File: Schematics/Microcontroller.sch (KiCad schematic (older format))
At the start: 25 parts, among them CON1 USB-MICRO-B, IC1 ATXMEGA256A3BU-A, J1 AVR_JTAG_Header, SW1 SW_PUSH, SW2 SW_PUSH, X1 16MHz, X2 32.768KhZ

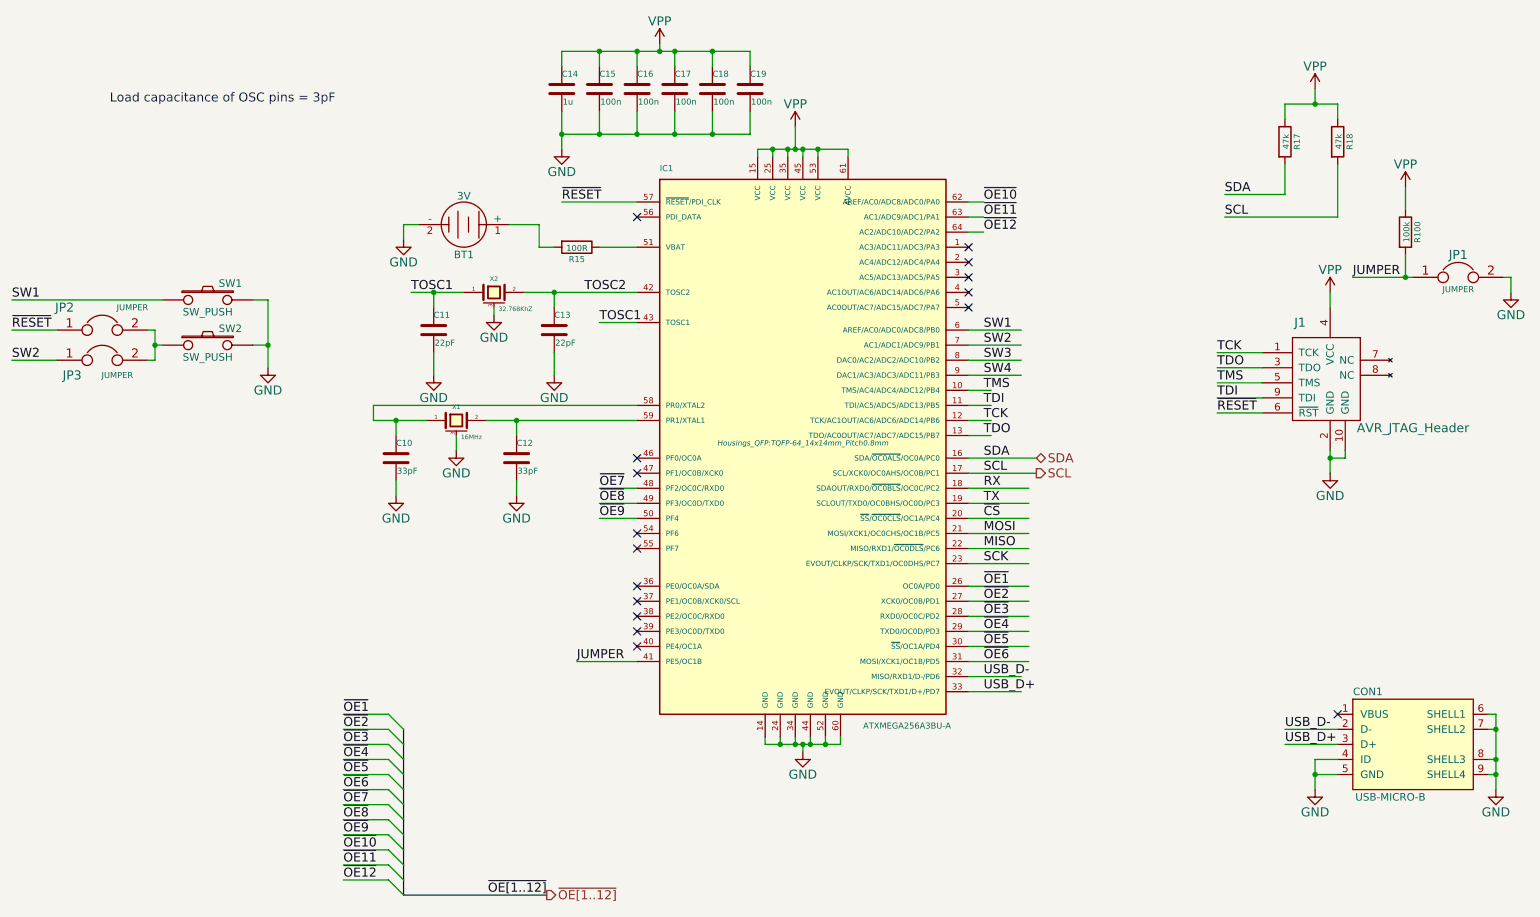
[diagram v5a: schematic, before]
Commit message: Split design into two modules
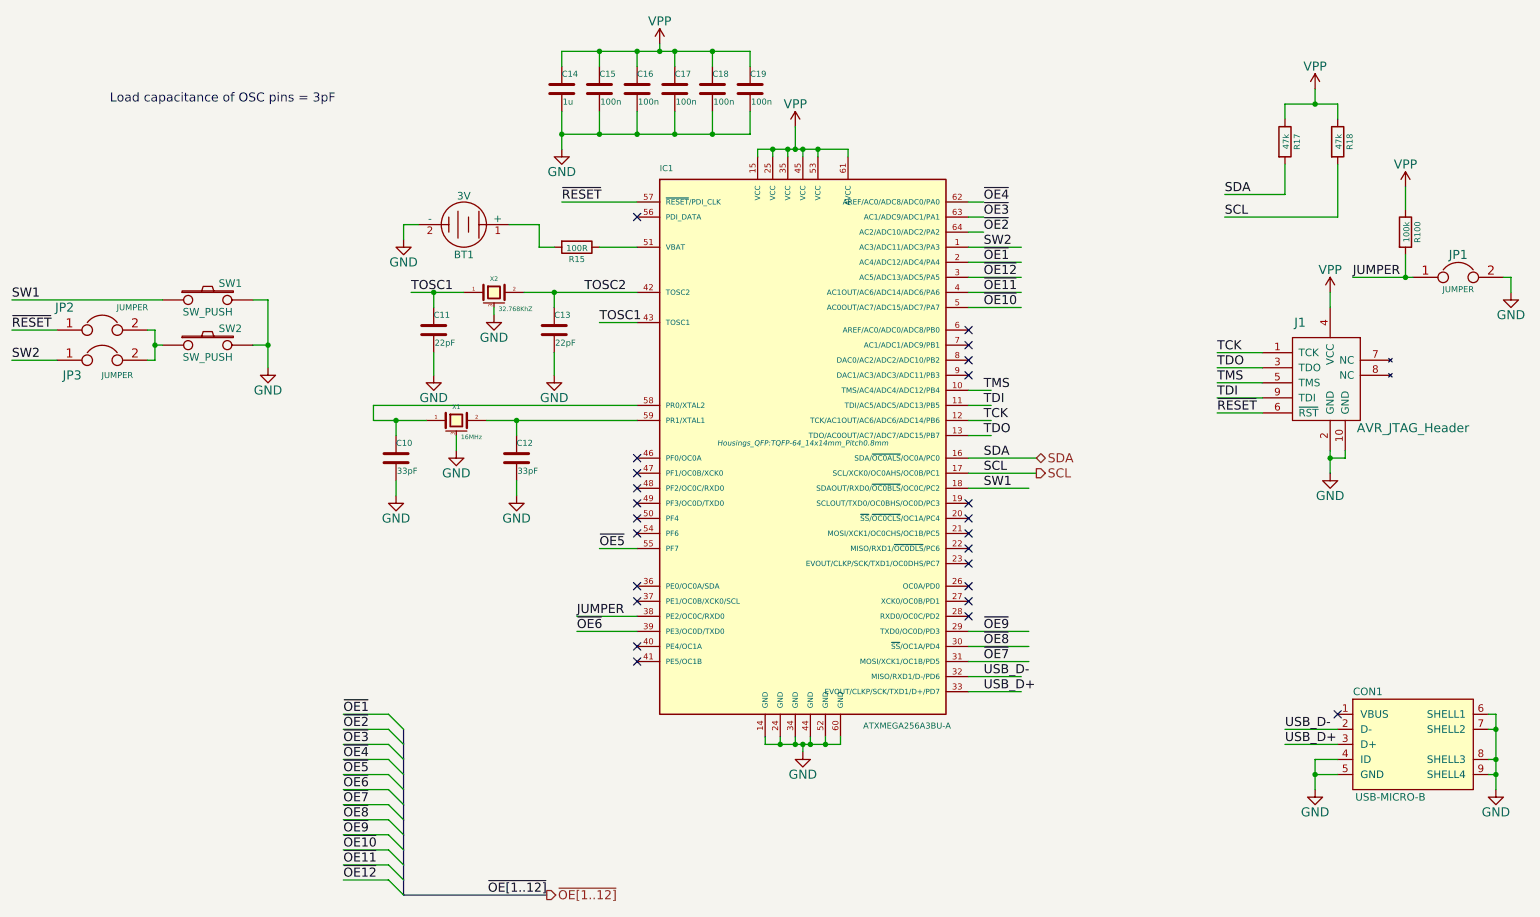
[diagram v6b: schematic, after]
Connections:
- net labels removed: MISO, MOSI, RX, SCK, SW3, SW4, TX, ~CS
- wire segments 174 -> 133
- no-connect marks 16 -> 24
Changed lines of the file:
@@
 	1    0    0    -1
 $EndComp
-Text Label 7050 4500 0    60   ~ 0
+Text Label 7050 2350 0    60   ~ 0
 ~OE1
-Text Label 7050 4600 0    60   ~ 0
+Text Label 7050 2150 0    60   ~ 0
 ~OE2
-Text Label 7050 4700 0    60   ~ 0
+Text Label 7050 2050 0    60   ~ 0
 ~OE3
+Text Label 7050 1950 0    60   ~ 0
+~OE4
+Text Label 4500 4250 0    60   ~ 0
+~OE5
+Text Label 4350 4800 0    60   ~ 0
+~OE6
+Text Label 7050 5000 0    60   ~ 0
+~OE7
+Text Label 7050 4900 0    60   ~ 0
+~OE8
 Text Label 7050 4800 0    60   ~ 0
-~OE4
-Text Label 7050 4900 0    60   ~ 0
-~OE5
-Text Label 7050 5000 0    60   ~ 0
-~OE6
-Text Label 4500 3850 0    60   ~ 0
-~OE7
-Text Label 4500 3950 0    60   ~ 0
-~OE8
-Text Label 4500 4050 0    60   ~ 0
 ~OE9
-Text Label 7050 1950 0    60   ~ 0
+Text Label 7050 2650 0    60   ~ 0
 ~OE10
-Text Label 7050 2050 0    60   ~ 0
+Text Label 7050 2550 0    60   ~ 0
 ~OE11
-Text Label 7050 2150 0    60   ~ 0
+Text Label 7050 2450 0    60   ~ 0
 ~OE12
 Entry Wire Line
@@
 	1    0    0    -1
 $EndComp
-Text Label 7050 4350 0    60   ~ 0
-SCK
-Text Label 7050 4250 0    60   ~ 0
-MISO
-Text Label 7050 4150 0    60   ~ 0
-MOSI
-Text Label 7050 4050 0    60   ~ 0
-~CS
-Text Label 7050 3950 0    60   ~ 0
-TX
-Text Label 7050 3850 0    60   ~ 0
-RX
-NoConn ~ 4750 4250
 NoConn ~ 4750 4150
 NoConn ~ 4750 3750
 NoConn ~ 4750 3650
-NoConn ~ 6950 2450
 NoConn ~ 9400 5350
 $Comp
@@
 	9050 1700 9050 1900
 Wire Wire Line
-	9050 1300 9250 1300
-Wire Wire Line
-	9250 1300 9400 1300
+	9050 1300 9400 1300
 Wire Wire Line
 	9250 1300 9250 1200
@@
 	5550 1650 5550 1600
 Wire Wire Line
-	5550 1600 5650 1600
-Wire Wire Line
-	5650 1600 5750 1600
-Wire Wire Line
-	5750 1600 5800 1600
-Wire Wire Line
-	5800 1600 5850 1600
-Wire Wire Line
-	5850 1600 5950 1600
-Wire Wire Line
-	5950 1600 6150 1600
+	5550 1600 6150 1600
 Wire Wire Line
 	6150 1600 6150 1650
@@
 	5600 5500 5600 5550
 Wire Wire Line
-	5600 5550 5700 5550
-Wire Wire Line
-	5700 5550 5800 5550
-Wire Wire Line
-	5800 5550 5850 5550
-Wire Wire Line
-	5850 5550 5900 5550
-Wire Wire Line
-	5900 5550 6000 5550
-Wire Wire Line
-	6000 5550 6100 5550
+	5600 5550 6100 5550
 Wire Wire Line
 	6100 5550 6100 5500
@@
 Connection ~ 5850 5550
 Wire Bus Line
-	3200 5450 3200 5550
-Wire Bus Line
-	3200 5550 3200 5650
-Wire Bus Line
-	3200 5650 3200 5750
-Wire Bus Line
-	3200 5750 3200 5850
-Wire Bus Line
-	3200 5850 3200 5950
-Wire Bus Line
-	3200 5950 3200 6050
-Wire Bus Line
-	3200 6050 3200 6150
-Wire Bus Line
-	3200 6150 3200 6250
-Wire Bus Line
-	3200 6250 3200 6350
-Wire Bus Line
-	3200 6350 3200 6450
-Wire Bus Line
-	3200 6450 3200 6550
+	3200 5450 3200 6550
 Wire Bus Line
 	3200 6550 4150 6550
 Wire Wire Line
-	7350 5000 6950 5000
-Wire Wire Line
-	7350 4600 6950 4600
-Wire Wire Line
-	6950 4500 7350 4500
-Wire Wire Line
 	6950 3500 7100 3500
 Wire Wire Line
@@
 	8600 3350 8900 3350
 Wire Wire Line
-	9350 3600 9350 3650
-Wire Wire Line
-	9350 3650 9350 3750
+	9350 3600 9350 3750
 Wire Wire Line
 	9350 3650 9450 3650
@@
 	4250 1950 4750 1950
 Wire Wire Line
-	4000 2550 4200 2550
-Wire Wire Line
-	4200 2550 4750 2550
+	4000 2550 4750 2550
 Connection ~ 4200 2550
 Wire Wire Line
@@
 	3400 2550 3400 2650
 Wire Wire Line
-	3250 2550 3400 2550
-Wire Wire Line
-	3400 2550 3600 2550
+	3250 2550 3600 2550
 Connection ~ 3400 2550
 Wire Wire Line
@@
 	3150 3400 3150 3500
 Wire Wire Line
-	3000 3400 3150 3400
-Wire Wire Line
-	3150 3400 3350 3400
+	3000 3400 3350 3400
 Connection ~ 3150 3400
 Wire Wire Line
@@
 	3150 3800 3150 3900
 Wire Wire Line
-	3750 3400 3950 3400
-Wire Wire Line
-	3950 3400 4750 3400
+	3750 3400 4750 3400
 Wire Wire Line
 	3000 3300 4750 3300
@@
 	9050 5550 9400 5550
 Wire Wire Line
-	10450 5350 10450 5450
-Wire Wire Line
-	10450 5450 10450 5650
-Wire Wire Line
-	10450 5650 10450 5750
-Wire Wire Line
-	10450 5750 10450 5850
+	10450 5350 10450 5850
 Wire Wire Line
 	10450 5350 10400 5350
@@
 	9400 5650 9250 5650
 Wire Wire Line
-	9250 5650 9250 5750
-Wire Wire Line
-	9250 5750 9250 5850
+	9250 5650 9250 5850
 Wire Wire Line
 	9400 5750 9250 5750
@@
 	4250 950  4250 1050
 Wire Wire Line
-	4250 950  4500 950
-Wire Wire Line
-	4500 950  4750 950
-Wire Wire Line
-	4750 950  4900 950
-Wire Wire Line
-	4900 950  5000 950
-Wire Wire Line
-	5000 950  5250 950
-Wire Wire Line
-	5250 950  5500 950
+	4250 950  5500 950
 Wire Wire Line
 	5500 950  5500 1050
@@
 Connection ~ 4900 950
 Wire Wire Line
-	4250 1350 4250 1500
-Wire Wire Line
-	4250 1500 4250 1600
-Wire Wire Line
-	5500 1500 5250 1500
-Wire Wire Line
-	5250 1500 5000 1500
-Wire Wire Line
-	5000 1500 4750 1500
-Wire Wire Line
-	4750 1500 4500 1500
-Wire Wire Line
-	4500 1500 4250 1500
-Wire Wire Line
-	5500 1350 5500 1500
+	4250 1350 4250 1600
+Wire Wire Line
+	4250 1500 5500 1500
+Wire Wire Line
+	5500 1500 5500 1350
 Wire Wire Line
 	5250 1350 5250 1500
@@
 	9850 1850 9850 2000
 Wire Wire Line
-	9500 2450 9850 2450
-Wire Wire Line
-	9850 2450 9900 2450
+	9500 2450 9900 2450
 Wire Wire Line
 	9850 2300 9850 2450
@@
 	10550 2450 10500 2450
 Wire Wire Line
-	6950 3850 7350 3850
-Wire Wire Line
-	6950 3950 7350 3950
-Wire Wire Line
-	6950 4050 7350 4050
-Wire Wire Line
-	6950 4150 7350 4150
-Wire Wire Line
-	6950 4250 7350 4250
-Wire Wire Line
-	6950 4350 7350 4350
-Wire Wire Line
 	3000 3300 3000 3400
 Wire Wire Line
 	7350 3750 7350 3750
 Wire Wire Line
-	6950 3100 7300 3100
-Wire Wire Line
-	7300 3000 6950 3000
-Wire Wire Line
-	6950 2900 7300 2900
-Wire Wire Line
-	7300 2800 6950 2800
-Wire Wire Line
 	2200 2600 2300 2600
 Wire Wire Line
-	2300 2600 2300 2900
-Wire Wire Line
-	2300 2900 2300 3050
+	2300 2600 2300 3050
 Wire Wire Line
 	2200 2900 2300 2900
@@
 	1    0    0    -1
 $EndComp
-Wire Wire Line
-	4350 5000 4750 5000
 Text Label 9500 2450 0    60   ~ 0
 JUMPER
-Text Label 4350 5000 0    60   ~ 0
+Text Label 4350 4700 0    60   ~ 0
 JUMPER
-$Comp
-L ATXMEGA256A3BU-A IC1
-U 1 1 54B11B55
-P 5850 3550
-F 0 "IC1" H 4900 5350 40  0000 L BNN
-F 1 "ATXMEGA256A3BU-A" H 6250 1650 40  0000 L BNN
-F 2 "Housings_QFP:TQFP-64_14x14mm_Pitch0.8mm" H 5850 3550 35  0000 C CIN
-F 3 "" H 5850 3550 60  0000 C CNN
-F 4 "ATXMEGA256A3BU-A" H 5850 3550 60  0001 C CNN "Part"
-F 5 "Farnell" H 5850 3550 60  0001 C CNN "Supplier"
-	1    5850 3550
-	1    0    0    -1
-$EndComp
 Wire Wire Line
 	6950 4900 7350 4900
 Wire Wire Line
 	7350 4800 6950 4800
-Wire Wire Line
-	6950 4700 7350 4700
-Wire Wire Line
-	4750 3850 4500 3850
-Wire Wire Line
-	4500 3950 4750 3950
-Wire Wire Line
-	4750 4050 4500 4050
 Wire Wire Line
 	6950 2150 7050 2150
@@
 ~OE12
 NoConn ~ 4750 4900
-NoConn ~ 4750 4800
-NoConn ~ 4750 4700
 NoConn ~ 4750 4600
 NoConn ~ 4750 4500
-NoConn ~ 6950 2650
-NoConn ~ 6950 2550
-NoConn ~ 6950 2350
-NoConn ~ 6950 2250
 $Comp
 L JUMPER JP3
@@
 	1    0    0    -1
 $EndComp
-Text Label 7050 2800 0    60   ~ 0
+Text Label 7050 3850 0    60   ~ 0
 SW1
-Text Label 7050 2900 0    60   ~ 0
+Text Label 7050 2250 0    60   ~ 0
 SW2
-Text Label 7050 3000 0    60   ~ 0
-SW3
-Text Label 7050 3100 0    60   ~ 0
-SW4
 $Comp
 L JUMPER JP2
@@
 	1550 3000 1500 3000
 Wire Wire Line
-	1550 2800 1550 2900
-Wire Wire Line
-	1550 2900 1550 3000
+	1550 2800 1550 3000
 Wire Wire Line
 	1550 2900 1600 2900
@@
 	9400 1300 9400 1400
 $Comp
-L GND #PWR046
+L GND #PWR045
 U 1 1 54C97F8A
 P 2300 3050
-F 0 "#PWR046" H 2300 2800 60  0001 C CNN
+F 0 "#PWR045" H 2300 2800 60  0001 C CNN
 F 1 "GND" H 2300 2900 60  0000 C CNN
 F 2 "" H 2300 3050 60  0000 C CNN
@@
 	1    0    0    -1
 $EndComp
+Wire Wire Line
+	4350 4700 4750 4700
+NoConn ~ 4750 5000
+Wire Wire Line
+	4350 4800 4750 4800
+Wire Wire Line
+	7350 5000 6950 5000
+Wire Wire Line
+	6950 2650 7300 2650
+Wire Wire Line
+	6950 2550 7300 2550
+Wire Wire Line
+	6950 2450 7300 2450
+Wire Wire Line
+	7300 2350 6950 2350
+NoConn ~ 4750 3950
+NoConn ~ 4750 4050
+NoConn ~ 6950 4700
+NoConn ~ 6950 4600
+NoConn ~ 6950 4500
+NoConn ~ 6950 3100
+NoConn ~ 6950 3000
+$Comp
+L ATXMEGA256A3BU-A IC1
+U 1 1 54B11B55
+P 5850 3550
+F 0 "IC1" H 4900 5350 40  0000 L BNN
+F 1 "ATXMEGA256A3BU-A" H 6250 1650 40  0000 L BNN
+F 2 "Housings_QFP:TQFP-64_14x14mm_Pitch0.8mm" H 5850 3550 35  0000 C CIN
+F 3 "" H 5850 3550 60  0000 C CNN
+F 4 "ATXMEGA256A3BU-A" H 5850 3550 60  0001 C CNN "Part"
+F 5 "Farnell" H 5850 3550 60  0001 C CNN "Supplier"
+	1    5850 3550
+	1    0    0    -1
+$EndComp
+Wire Wire Line
+	4500 4250 4750 4250
+NoConn ~ 4750 3850
+Wire Wire Line
+	6950 3850 7350 3850
+Wire Wire Line
+	6950 2250 7300 2250
+NoConn ~ 6950 2800
+NoConn ~ 6950 2900
+NoConn ~ 6950 4350
+NoConn ~ 6950 4250
+NoConn ~ 6950 4150
+NoConn ~ 6950 4050
+NoConn ~ 6950 3950
 $EndSCHEMATC
